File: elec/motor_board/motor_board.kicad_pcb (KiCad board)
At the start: 2 copper layers, 74.2 x 47.2 mm, 5 parts, among them IC1 HAL1506UA, J2 connector to driver board

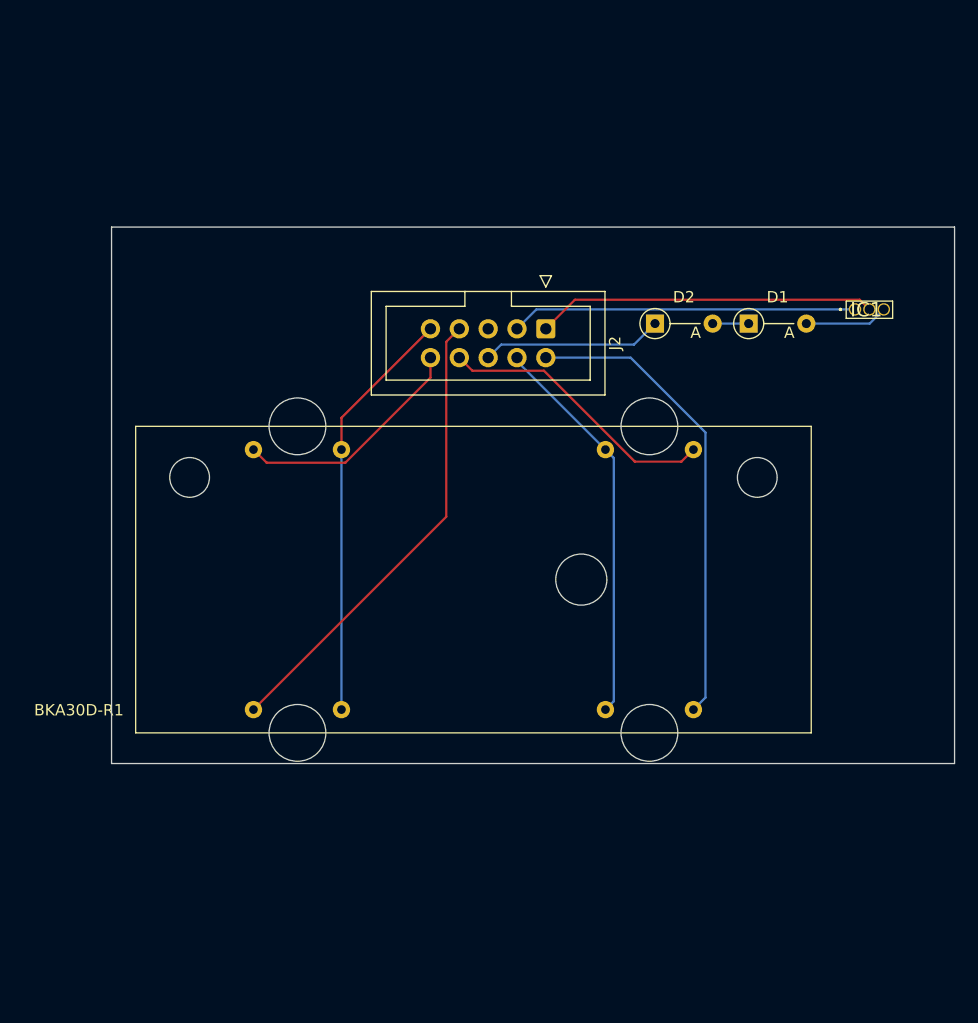
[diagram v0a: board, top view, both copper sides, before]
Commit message: [elec] continue routing
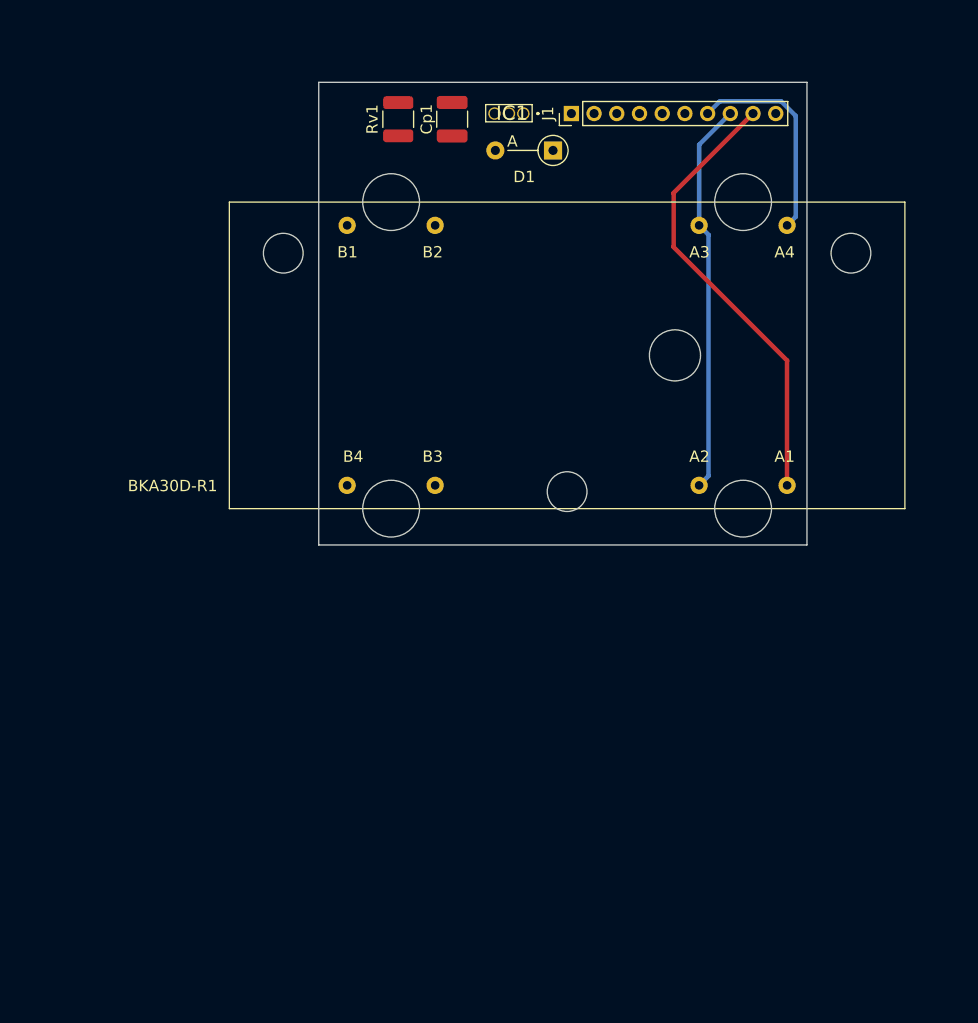
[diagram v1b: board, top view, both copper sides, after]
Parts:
- removed D2: 1N4148, Diode_THT:D_DO-35_SOD27_P5.08mm_Vertical_AnodeUp
- removed J2: connector to driver board, Connector_IDC:IDC-Header_2x05_P2.54mm_Vertical
- added Cp1: 10nF, Capacitor_SMD:C_1210_3225Metric, F.Cu at (173.0, 35.5)
- added J1: connector to driver board, Connector_PinHeader_2.00mm:PinHeader_1x10_P2.00mm_Vertical, F.Cu at (183.5, 35.0)
- added Rv1: 100Ω, Resistor_SMD:R_1210_3225Metric, F.Cu at (168.2, 35.5)
- IC1: value HAL1506UA -> HAL1503UA-A
- moved IC1 33.9 mm to (179.3, 35.0), turned to 180 degrees
- moved D1 23.0 mm to (181.9, 38.2), turned to 180 degrees
- moved BKA30D-R1 21.4 mm to (153.4, 69.8)
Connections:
- D1 pad 1: Net-(D1-K) -> /HALL_OUT
- IC1 pad 1: /VCC_HALL -> Net-(IC1-VCC)
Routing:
- net /M1_4: track 41.0 -> 0.00 mm
- net /M1_23: track 36.8 -> 0.00 mm
- net /VCC_HALL: track 30.5 -> 0.00 mm
- net GND: track 29.9 -> 0.00 mm
- net /M1_1: track 20.9 -> 0.00 mm
- net /HALL_OUT: track 15.9 -> 0.00 mm
- net Net-(D1-A): track 7.34 -> 0.00 mm
- net /M0_4: track 24.9 -> 18.7 mm
- net Net-(D1-K): track 3.17 -> 0.00 mm
- net /M0_1: track 41.6 -> 39.8 mm
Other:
- board size 74.2 x 47.2 mm -> 43 x 40.8 mm

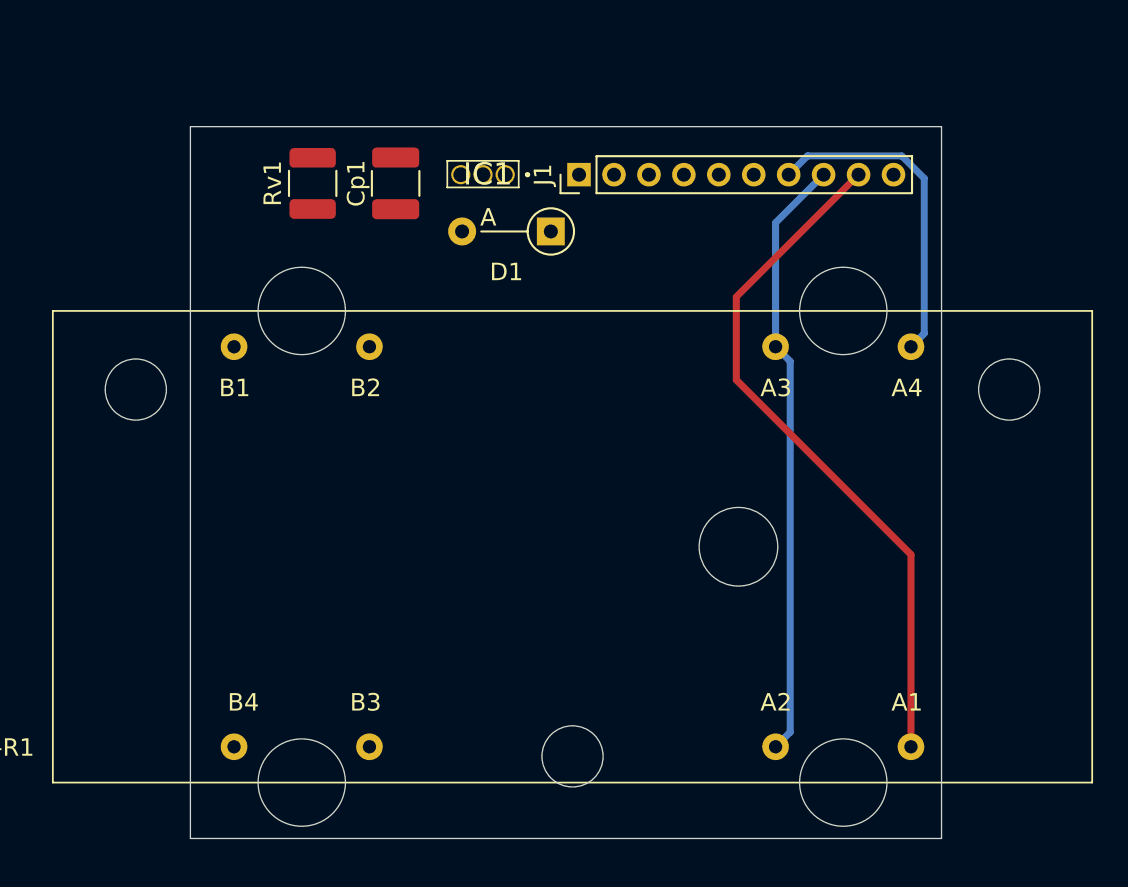
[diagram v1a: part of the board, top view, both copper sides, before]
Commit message: [elec] Add one more hall sensor
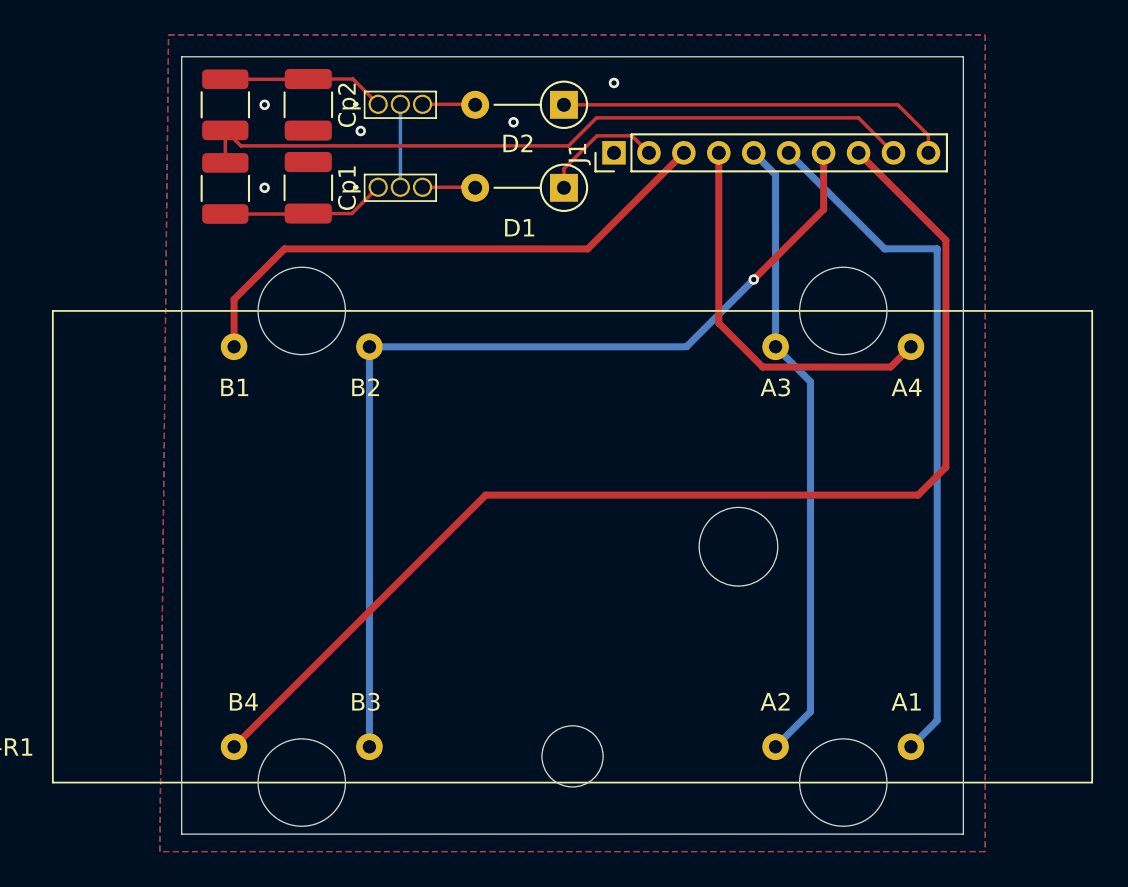
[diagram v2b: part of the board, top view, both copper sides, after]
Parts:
- added Cp2: 10nF, Capacitor_SMD:C_1210_3225Metric, F.Cu at (168.0, 31.0)
- added D2: 1N4148, Diode_THT:D_DO-35_SOD27_P5.08mm_Vertical_AnodeUp, F.Cu at (182.6, 31.0)
- added IC2: HAL1503UA-A, Samacsys:A1101EUAT, F.Cu at (172.0, 31.0)
- added Rv2: 100Ω, Resistor_SMD:R_1210_3225Metric, F.Cu at (163.2, 31.0)
- moved IC1 7.31 mm to (172.0, 35.7), turned to 0 degrees
- moved Rv1 5.01 mm to (163.2, 35.8), turned to -90 degrees
- moved Cp1 5.01 mm to (168.0, 35.8), turned to 90 degrees
- moved D1 2.61 mm to (182.6, 35.8)
- moved J1 2.36 mm to (185.5, 33.8)
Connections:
- D1 pad 1: /HALL_OUT -> /HALL_0_OUT
- J1 pad 10: unconnected-(J1-Pin_10-Pad10) -> /HALL_1_OUT
- J1 pad 2: VCC -> /HALL_0_OUT
- J1 pad 3: /HALL_OUT -> /M1_1
- J1 pad 4: /M1_1 -> /M0_4
- J1 pad 5: /M1_23 -> /M0_23
- J1 pad 6: /M1_4 -> /M0_1
- J1 pad 7: /M0_4 -> /M1_23
- J1 pad 8: /M0_23 -> /M1_4
- J1 pad 9: /M0_1 -> VCC
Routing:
- net /M1_4: track 0.00 -> 67.4 mm
- net /M1_23: track 0.00 -> 55.4 mm, vias 0 -> 1
- net VCC: track 0.00 -> 42.0 mm
- net /M1_1: track 0.00 -> 31.9 mm
- net /HALL_1_OUT: track 0.00 -> 22.6 mm
- net Net-(IC1-VCC): track 0.00 -> 9.38 mm
- net Net-(IC2-VCC): track 0.00 -> 9.35 mm
- net /HALL_0_OUT: track 0.00 -> 7.14 mm
- net GND: track 0.00 -> 4.75 mm, vias 0 -> 5
- net /M0_4: track 18.7 -> 22.3 mm
- net Net-(D2-A): track 0.00 -> 3.03 mm
- net Net-(D1-A): track 0.00 -> 3.03 mm
- net /M0_23: track 34.6 -> 36.2 mm
- added copper zone on B.Cu, net GND
- added copper zone on F.Cu, net GND
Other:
- board size 43 x 40.8 mm -> 44.8 x 44.5 mm

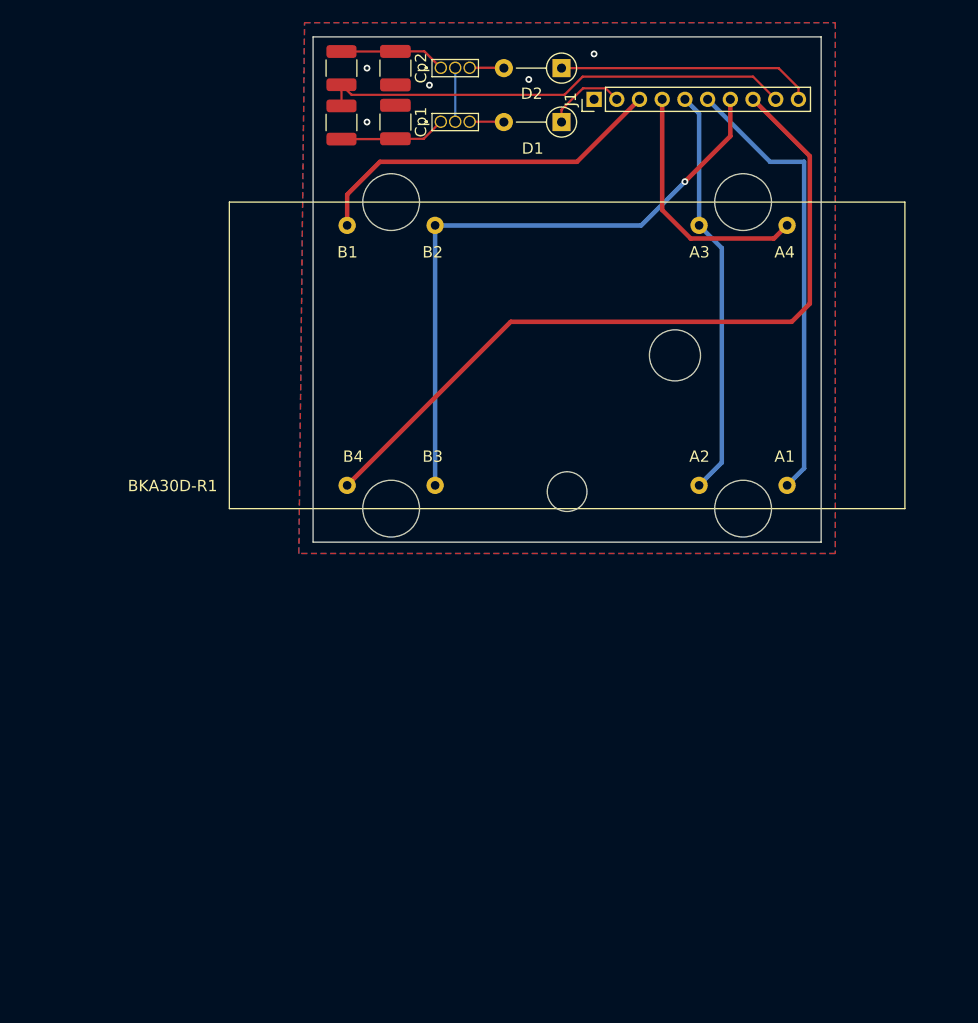
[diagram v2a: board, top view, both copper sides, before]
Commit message: Update BKA30D-R5 dimensions
Also add some silkscreen on both PCB
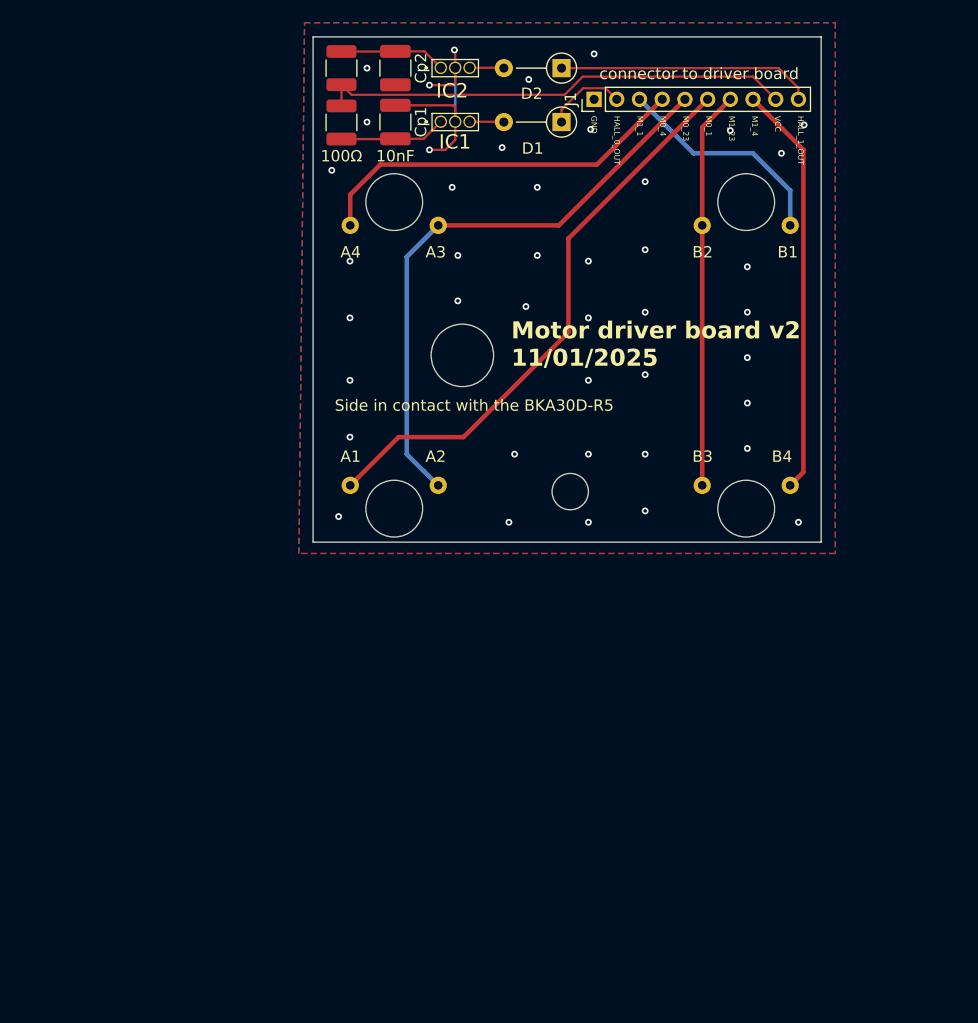
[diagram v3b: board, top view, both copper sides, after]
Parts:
- BKA30D-R1: moved to B.Cu
- moved BKA30D-R1 59.8 mm to (213.2, 69.8), turned to 180 degrees
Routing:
- net /M1_4: track 67.4 -> 36.3 mm
- net /M1_23: track 55.4 -> 35.0 mm, vias 1 -> 0
- net GND: track 4.75 -> 20.9 mm, vias 5 -> 43
- net /M0_23: track 36.2 -> 51.5 mm
- net /M1_1: track 31.9 -> 19.7 mm
- net /M0_4: track 22.3 -> 33.7 mm
- net /M0_1: track 39.9 -> 50.4 mm
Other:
- board text added: "GND"
- board text added: "HALL_0_OUT"
- board text added: "HALL_1_OUT"
- board text added: "M0_1"
- board text added: "M0_23"
- board text added: "M0_4"
- board text added: "M1_1"
- board text added: "M1_23"
- board text added: "M1_4"
- board text added: "Motor driver board v2 11/01/2025"
- board text added: "VCC"

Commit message: PCB done, ready to be ordered
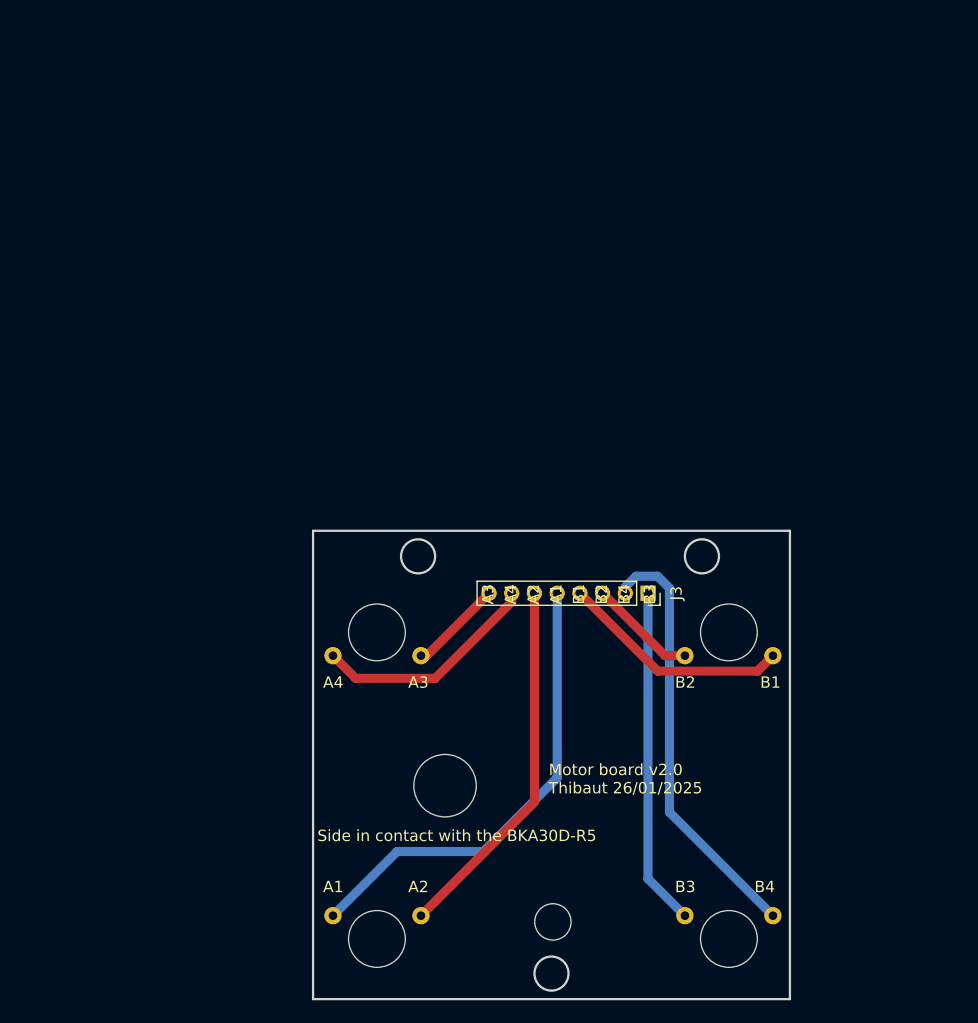
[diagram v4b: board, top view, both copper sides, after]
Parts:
- removed Cp1, Cp2: 10nF, Capacitor_SMD:C_1210_3225Metric
- removed D1, D2: 1N4148, Diode_THT:D_DO-35_SOD27_P5.08mm_Vertical_AnodeUp
- removed IC1, IC2: HAL1503UA-A, Samacsys:A1101EUAT
- removed J1: connector to driver board, Connector_PinHeader_2.00mm:PinHeader_1x10_P2.00mm_Vertical
- removed Rv1, Rv2: 100Ω, Resistor_SMD:R_1210_3225Metric
- added J3: Conn_01x08, Connector_PinSocket_2.00mm:PinSocket_1x08_P2.00mm_Vertical, F.Cu at (190.2, 77.2)
- moved BKA30D-R1 37.9 mm to (211.6, 107.7)
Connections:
- BKA30D-R1 pad A1: /M0_1 -> /A1
- BKA30D-R1 pad A2: /M0_23 -> /A2
- BKA30D-R1 pad A3: /M0_23 -> /A3
- BKA30D-R1 pad A4: /M0_4 -> /A4
- BKA30D-R1 pad B1: /M1_1 -> /B1
- BKA30D-R1 pad B2: /M1_23 -> /B2
- BKA30D-R1 pad B3: /M1_23 -> /B3
- BKA30D-R1 pad B4: /M1_4 -> /B4
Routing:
- net /M0_23: track 51.5 -> 0.00 mm
- net /M0_1: track 50.4 -> 0.00 mm
- net VCC: track 42.0 -> 0.00 mm
- net /A1: track 0.00 -> 41.0 mm
- net /B4: track 0.00 -> 37.9 mm
- net /M1_4: track 36.3 -> 0.00 mm
- net /M1_23: track 35.0 -> 0.00 mm
- net /M0_4: track 33.7 -> 0.00 mm
- net /A2: track 0.00 -> 32.5 mm
- net /B3: track 0.00 -> 29.7 mm
- net /HALL_1_OUT: track 22.6 -> 0.00 mm
- net GND: track 20.9 -> 0.00 mm, vias 43 -> 0
- net /B1: track 0.00 -> 20.4 mm
- net /A4: track 0.00 -> 20.1 mm
- net /M1_1: track 19.7 -> 0.00 mm
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- removed copper zone on B.Cu, net GND
- removed copper zone on F.Cu, net GND
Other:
- board size 44.8 x 44.5 mm -> 42 x 41.2 mm
- board text added: "A1"
- board text added: "A2"
- board text added: "A3"
- board text added: "A4"
- board text added: "B1"
- board text added: "B2"
- board text added: "B3"
- board text added: "B4"
- board text added: "Motor board v2.0 Thibaut 26/01/2025"
- board text removed: "GND"
- board text removed: "HALL_0_OUT"
- board text removed: "HALL_1_OUT"
- board text removed: "M0_1"
- board text removed: "M0_23"
- board text removed: "M0_4"
- board text removed: "M1_1"
- board text removed: "M1_23"
- board text removed: "M1_4"
- board text removed: "Motor driver board v2 11/01/2025"
- board text removed: "VCC"
